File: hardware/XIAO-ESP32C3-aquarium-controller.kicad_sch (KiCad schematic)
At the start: 11 parts, among them J1 Conn_01x07, J3 Conn_01x06, U1 XIAO-ESP32C3, U2 ULN2003, U3 74HC245

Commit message: added new connector, increase copper for al/n
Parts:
- added J2: Conn_01x03, Connector_PinHeader_2.54mm:PinHeader_1x05_P2.54mm_Vertical, symbol Connector_Generic:Conn_01x05
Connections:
- net +5V: now also J2.1 (Pin_1)
- net GND: now also J2.5 (Pin_5)
- net D2: now reaches U1.3 (PA10_A2_D2)
- net D2: now also J2.3 (Pin_3)
- net D6: now reaches U1.7 (PB08_A6_D6_TX)
- net D6: now also J2.4 (Pin_4)
- net D7: now reaches U1.8 (PB09_A7_D7_RX)
- net D7: now also J2.2 (Pin_2)
- no-connect marks 9 -> 6
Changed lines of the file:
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@@
   )
   (no_connect (at 144.78 121.92))
-  (no_connect (at 29.21 86.36))
   (no_connect (at 144.78 124.46))
   (no_connect (at 120.65 72.39))
-  (no_connect (at 29.21 101.6))
-  (no_connect (at 78.74 101.6))
   (no_connect (at 140.97 72.39))
   (no_connect (at 119.38 121.92))
@@
     (stroke (width 0) (type default))
   )
+  (wire (pts (xy 45.72 138.43) (xy 45.72 134.62))
+    (stroke (width 0) (type default))
+  )
+  (wire (pts (xy 45.72 121.92) (xy 45.72 124.46))
+    (stroke (width 0) (type default))
+  )
   (wire (pts (xy 119.38 116.84) (xy 119.38 119.38))
     (stroke (width 0) (type default))
@@
     (stroke (width 0) (type default))
   )
+  (wire (pts (xy 45.72 124.46) (xy 50.8 124.46))
+    (stroke (width 0) (type default))
+  )
   (wire (pts (xy 114.3 116.84) (xy 119.38 116.84))
     (stroke (width 0) (type default))
   )
+  (wire (pts (xy 25.4 86.36) (xy 29.21 86.36))
+    (stroke (width 0) (type default))
+  )
   (wire (pts (xy 222.25 127) (xy 227.33 127))
     (stroke (width 0) (type default))
@@
     (stroke (width 0) (type default))
   )
+  (wire (pts (xy 45.72 132.08) (xy 50.8 132.08))
+    (stroke (width 0) (type default))
+  )
+  (wire (pts (xy 78.74 101.6) (xy 82.55 101.6))
+    (stroke (width 0) (type default))
+  )
   (wire (pts (xy 219.71 119.38) (xy 227.33 119.38))
     (stroke (width 0) (type default))
@@
     (stroke (width 0) (type default))
   )
+  (wire (pts (xy 45.72 127) (xy 50.8 127))
+    (stroke (width 0) (type default))
+  )
   (wire (pts (xy 130.81 78.74) (xy 130.81 77.47))
     (stroke (width 0) (type default))
@@
     (stroke (width 0) (type default))
   )
+  (wire (pts (xy 45.72 134.62) (xy 50.8 134.62))
+    (stroke (width 0) (type default))
+  )
   (wire (pts (xy 119.38 69.85) (xy 119.38 67.31))
     (stroke (width 0) (type default))
@@
     (stroke (width 0) (type default))
   )
+  (wire (pts (xy 25.4 101.6) (xy 29.21 101.6))
+    (stroke (width 0) (type default))
+  )
   (wire (pts (xy 78.74 72.39) (xy 88.9 72.39))
     (stroke (width 0) (type default))
@@
     (stroke (width 0) (type default))
   )
+  (wire (pts (xy 45.72 129.54) (xy 50.8 129.54))
+    (stroke (width 0) (type default))
+  )
   (wire (pts (xy 119.38 132.08) (xy 119.38 139.7))
     (stroke (width 0) (type default))
@@
     (stroke (width 0) (type default))
   )
+  (label "D7" (at 45.72 127 0) (fields_autoplaced)
+    (effects (font (size 1.27 1.27)) (justify left bottom))
+  )
   (label "TS1" (at 177.8 25.4 0) (fields_autoplaced)
     (effects (font (size 1.27 1.27)) (justify left bottom))
@@
     (effects (font (size 1.27 1.27)) (justify left bottom))
   )
+  (label "D6" (at 25.4 101.6 0) (fields_autoplaced)
+    (effects (font (size 1.27 1.27)) (justify left bottom))
+  )
   (label "rel2" (at 177.8 68.58 0) (fields_autoplaced)
     (effects (font (size 1.27 1.27)) (justify left bottom))
@@
     (effects (font (size 1.27 1.27)) (justify left bottom))
   )
+  (label "D2" (at 25.4 86.36 0) (fields_autoplaced)
+    (effects (font (size 1.27 1.27)) (justify left bottom))
+  )
+  (label "D6" (at 45.72 132.08 0) (fields_autoplaced)
+    (effects (font (size 1.27 1.27)) (justify left bottom))
+  )
   (label "RS5" (at 115.57 67.31 0) (fields_autoplaced)
     (effects (font (size 1.27 1.27)) (justify left bottom))
@@
     (effects (font (size 1.27 1.27)) (justify left bottom))
   )
+  (label "D7" (at 82.55 101.6 0) (fields_autoplaced)
+    (effects (font (size 1.27 1.27)) (justify left bottom))
+  )
   (label "rel3" (at 143.51 67.31 0) (fields_autoplaced)
     (effects (font (size 1.27 1.27)) (justify left bottom))
@@
   )
   (label "RS1" (at 114.3 116.84 0) (fields_autoplaced)
+    (effects (font (size 1.27 1.27)) (justify left bottom))
+  )
+  (label "D2" (at 45.72 129.54 0) (fields_autoplaced)
     (effects (font (size 1.27 1.27)) (justify left bottom))
   )
@@
     )
   )
+  (symbol (lib_id "power:GND") (at 45.72 138.43 0) (unit 1)
+    (in_bom yes) (on_board yes) (dnp no) (fields_autoplaced)
+    (property "Reference" "#PWR0103" (at 45.72 144.78 0)
+      (effects (font (size 1.27 1.27)) hide)
+    )
+    (property "Value" "GND" (at 45.72 143.51 0)
+      (effects (font (size 1.27 1.27)))
+    )
+    (property "Footprint" "" (at 45.72 138.43 0)
+      (effects (font (size 1.27 1.27)) hide)
+    )
+    (property "Datasheet" "" (at 45.72 138.43 0)
+      (effects (font (size 1.27 1.27)) hide)
+    )
+    (pin "1")
+    (instances
+      (project "AquariumController"
+        (path "/75069d71-4fd1-4b49-820b-d8e60608591a"
+          (reference "#PWR0103") (unit 1)
+        )
+        (path "/75069d71-4fd1-4b49-820b-d8e60608591a/cae2cbae-b73f-4926-bf8f-e52abe478c81"
+          (reference "#PWR017") (unit 1)
+        )
+      )
+      (project "XIAO-ESP32C3-aquarium-controller"
+        (path "/e16639bd-7ef7-40a4-9337-f1b4c79f775b/bee5e875-31e5-4be6-8420-aaa58bd7d71a"
+          (reference "#PWR02") (unit 1)
+        )
+        (path "/e16639bd-7ef7-40a4-9337-f1b4c79f775b"
+          (reference "#PWR035") (unit 1)
+        )
+      )
+    )
+  )
   (symbol (lib_id "Device:C") (at 137.16 34.29 90) (unit 1)
     (in_bom yes) (on_board yes) (dnp no) (fields_autoplaced)
@@
         (path "/e16639bd-7ef7-40a4-9337-f1b4c79f775b"
           (reference "H1") (unit 1)
+        )
+      )
+    )
+  )
+  (symbol (lib_id "Connector_Generic:Conn_01x05") (at 55.88 129.54 0) (unit 1)
+    (in_bom no) (on_board yes) (dnp no) (fields_autoplaced)
+    (property "Reference" "J2" (at 58.42 128.27 0)
+      (effects (font (size 1.27 1.27)) (justify left))
+    )
+    (property "Value" "Conn_01x03" (at 58.42 130.81 0)
+      (effects (font (size 1.27 1.27)) (justify left))
+    )
+    (property "Footprint" "Connector_PinHeader_2.54mm:PinHeader_1x05_P2.54mm_Vertical" (at 55.88 129.54 0)
+      (effects (font (size 1.27 1.27)) hide)
+    )
+    (property "Datasheet" "~" (at 55.88 129.54 0)
+      (effects (font (size 1.27 1.27)) hide)
+    )
+    (property "JLCPCB Part #" "" (at 55.88 129.54 0)
+      (effects (font (size 1.27 1.27)) hide)
+    )
+    (pin "1")
+    (pin "2")
+    (pin "3")
+    (pin "4")
+    (pin "5")
+    (instances
+      (project "AquariumController"
+        (path "/75069d71-4fd1-4b49-820b-d8e60608591a/5fd9d187-6c53-4498-b6f0-99546b3ca792"
+          (reference "J2") (unit 1)
+        )
+      )
+      (project "XIAO-ESP32C3-aquarium-controller"
+        (path "/e16639bd-7ef7-40a4-9337-f1b4c79f775b/6cb334e1-33ef-41c6-b7ff-62ff02100eaa"
+          (reference "J4") (unit 1)
+        )
+        (path "/e16639bd-7ef7-40a4-9337-f1b4c79f775b"
+          (reference "J5") (unit 1)
         )
       )
@@
         )
       )
+    )
+  )
+  (symbol (lib_id "power:+5V") (at 45.72 121.92 0) (unit 1)
+    (in_bom yes) (on_board yes) (dnp no) (fields_autoplaced)
+    (property "Reference" "#PWR0102" (at 45.72 125.73 0)
+      (effects (font (size 1.27 1.27)) hide)
+    )
+    (property "Value" "+5V" (at 45.72 116.84 0)
+      (effects (font (size 1.27 1.27)))
+    )
+    (property "Footprint" "" (at 45.72 121.92 0)
+      (effects (font (size 1.27 1.27)) hide)
+    )
+    (property "Datasheet" "" (at 45.72 121.92 0)
+      (effects (font (size 1.27 1.27)) hide)
+    )
+    (pin "1")
+    (instances
+      (project "AquariumController"
+        (path "/75069d71-4fd1-4b49-820b-d8e60608591a"
+          (reference "#PWR0102") (unit 1)
+        )
+        (path "/75069d71-4fd1-4b49-820b-d8e60608591a/cae2cbae-b73f-4926-bf8f-e52abe478c81"
+          (reference "#PWR016") (unit 1)
+        )
+      )
+      (project "XIAO-ESP32C3-aquarium-controller"
+        (path "/e16639bd-7ef7-40a4-9337-f1b4c79f775b/bee5e875-31e5-4be6-8420-aaa58bd7d71a"
+          (reference "#PWR01") (unit 1)
+        )
+        (path "/e16639bd-7ef7-40a4-9337-f1b4c79f775b"
+          (reference "#PWR034") (unit 1)
+        )
+      )

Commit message: 3v3 instead 5v on connector
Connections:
- net +3.3V: now also J2.1 (Pin_1)
- net +5V: no longer J2.1 (Pin_1)
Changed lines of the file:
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@@
+    )
+  )
+  (symbol (lib_id "power:+3.3V") (at 45.72 121.92 0) (unit 1)
+    (in_bom yes) (on_board yes) (dnp no) (fields_autoplaced)
+    (property "Reference" "#PWR029" (at 45.72 125.73 0)
+      (effects (font (size 1.27 1.27)) hide)
+    )
+    (property "Value" "+3.3V" (at 45.72 118.11 0)
+      (effects (font (size 1.27 1.27)))
+    )
+    (property "Footprint" "" (at 45.72 121.92 0)
+      (effects (font (size 1.27 1.27)) hide)
+    )
+    (property "Datasheet" "" (at 45.72 121.92 0)
+      (effects (font (size 1.27 1.27)) hide)
+    )
+    (pin "1")
+    (instances
+      (project "AquariumController"
+        (path "/75069d71-4fd1-4b49-820b-d8e60608591a/cae2cbae-b73f-4926-bf8f-e52abe478c81"
+          (reference "#PWR029") (unit 1)
+        )
+        (path "/75069d71-4fd1-4b49-820b-d8e60608591a"
+          (reference "#PWR031") (unit 1)
+        )
+        (path "/75069d71-4fd1-4b49-820b-d8e60608591a/5fd9d187-6c53-4498-b6f0-99546b3ca792"
+          (reference "#PWR014") (unit 1)
+        )
+      )
+      (project "XIAO-ESP32C3-aquarium-controller"
+        (path "/e16639bd-7ef7-40a4-9337-f1b4c79f775b/6cb334e1-33ef-41c6-b7ff-62ff02100eaa"
+          (reference "#PWR029") (unit 1)
+        )
+        (path "/e16639bd-7ef7-40a4-9337-f1b4c79f775b"
+          (reference "#PWR034") (unit 1)
+        )
+      )
     )
   )
@@
         )
       )
-    )
-  )
-  (symbol (lib_id "power:+5V") (at 45.72 121.92 0) (unit 1)
-    (in_bom yes) (on_board yes) (dnp no) (fields_autoplaced)
-    (property "Reference" "#PWR0102" (at 45.72 125.73 0)
-      (effects (font (size 1.27 1.27)) hide)
-    )
-    (property "Value" "+5V" (at 45.72 116.84 0)
-      (effects (font (size 1.27 1.27)))
-    )
-    (property "Footprint" "" (at 45.72 121.92 0)
-      (effects (font (size 1.27 1.27)) hide)
-    )
-    (property "Datasheet" "" (at 45.72 121.92 0)
-      (effects (font (size 1.27 1.27)) hide)
-    )
-    (pin "1")
-    (instances
-      (project "AquariumController"
-        (path "/75069d71-4fd1-4b49-820b-d8e60608591a"
-          (reference "#PWR0102") (unit 1)
-        )
-        (path "/75069d71-4fd1-4b49-820b-d8e60608591a/cae2cbae-b73f-4926-bf8f-e52abe478c81"
-          (reference "#PWR016") (unit 1)
-        )
-      )
-      (project "XIAO-ESP32C3-aquarium-controller"
-        (path "/e16639bd-7ef7-40a4-9337-f1b4c79f775b/bee5e875-31e5-4be6-8420-aaa58bd7d71a"
-          (reference "#PWR01") (unit 1)
-        )
-        (path "/e16639bd-7ef7-40a4-9337-f1b4c79f775b"
-          (reference "#PWR034") (unit 1)
-        )
-      )

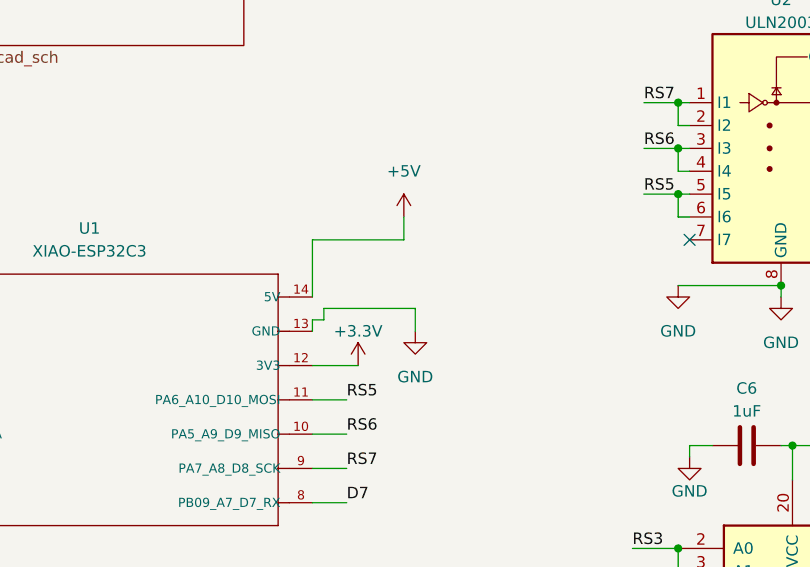
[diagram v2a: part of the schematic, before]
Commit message: capacitor for ESP32C3
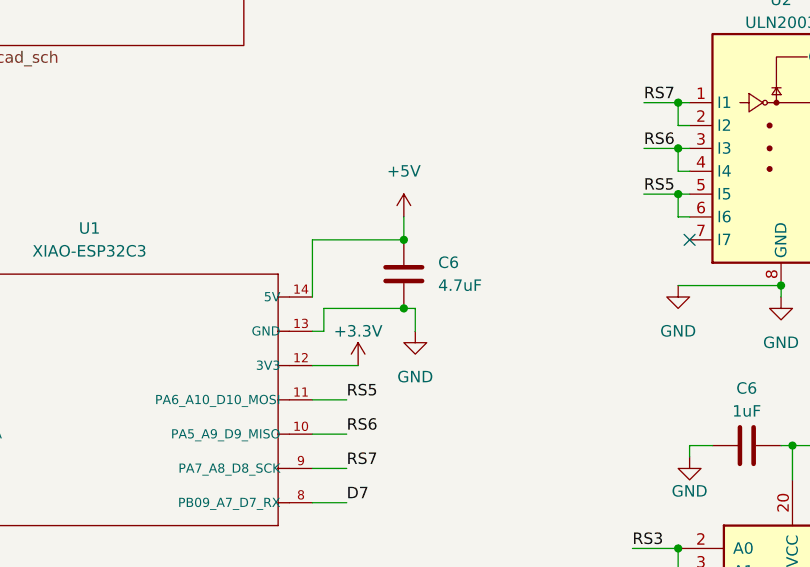
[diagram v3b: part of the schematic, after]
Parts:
- added C6: 4.7uF, Capacitor_SMD:C_0402_1005Metric, symbol Device:C
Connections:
- net +5V: now also C6.2
- net GND: now also C6.1
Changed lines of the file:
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@@
   (junction (at 119.38 57.15) (diameter 0) (color 0 0 0 0)
   )
+  (junction (at 88.9 72.39) (diameter 0) (color 0 0 0 0)
+  )
   (junction (at 119.38 106.68) (diameter 0) (color 0 0 0 0)
   )
@@
   )
   (junction (at 144.78 111.76) (diameter 0) (color 0 0 0 0)
+  )
+  (junction (at 88.9 80.01) (diameter 0) (color 0 0 0 0)
   )
   (junction (at 142.24 62.23) (diameter 0) (color 0 0 0 0)
@@
     (stroke (width 0) (type default))
   )
+  (wire (pts (xy 88.9 80.01) (xy 90.17 80.01))
+    (stroke (width 0) (type default))
+  )
   (wire (pts (xy 143.51 67.31) (xy 142.24 67.31))
     (stroke (width 0) (type default))
@@
     (stroke (width 0) (type default))
   )
-  (wire (pts (xy 78.74 81.28) (xy 78.74 82.55))
+  (wire (pts (xy 80.01 80.01) (xy 80.01 82.55))
     (stroke (width 0) (type default))
   )
@@
     (stroke (width 0) (type default))
   )
+  (wire (pts (xy 80.01 82.55) (xy 78.74 82.55))
+    (stroke (width 0) (type default))
+  )
   (wire (pts (xy 204.47 85.09) (xy 220.98 85.09))
     (stroke (width 0) (type default))
@@
     (stroke (width 0) (type default))
   )
-  (wire (pts (xy 80.01 81.28) (xy 78.74 81.28))
-    (stroke (width 0) (type default))
-  )
   (wire (pts (xy 219.71 106.68) (xy 219.71 119.38))
     (stroke (width 0) (type default))
@@
     (stroke (width 0) (type default))
   )
-  (wire (pts (xy 80.01 80.01) (xy 90.17 80.01))
+  (wire (pts (xy 80.01 80.01) (xy 88.9 80.01))
     (stroke (width 0) (type default))
   )
@@
   )
   (wire (pts (xy 132.08 95.25) (xy 148.59 95.25))
-    (stroke (width 0) (type default))
-  )
-  (wire (pts (xy 80.01 81.28) (xy 80.01 80.01))
     (stroke (width 0) (type default))
   )
@@
         )
       )
+    )
+  )
+  (symbol (lib_id "Device:C") (at 88.9 76.2 180) (unit 1)
+    (in_bom yes) (on_board yes) (dnp no) (fields_autoplaced)
+    (property "Reference" "C6" (at 92.71 74.93 0)
+      (effects (font (size 1.27 1.27)) (justify right))
+    )
+    (property "Value" "4.7uF" (at 92.71 77.47 0)
+      (effects (font (size 1.27 1.27)) (justify right))
+    )
+    (property "Footprint" "Capacitor_SMD:C_0402_1005Metric" (at 87.9348 72.39 0)
+      (effects (font (size 1.27 1.27)) hide)
+    )
+    (property "Datasheet" "~" (at 88.9 76.2 0)
+      (effects (font (size 1.27 1.27)) hide)
+    )
+    (property "JLCPCB Part #" "C23733" (at 88.9 76.2 0)
+      (effects (font (size 1.27 1.27)) hide)
+    )
+    (pin "1")
+    (pin "2")
+    (instances
+      (project "AquariumController"
+        (path "/75069d71-4fd1-4b49-820b-d8e60608591a"
+          (reference "C6") (unit 1)
+        )
+      )
+      (project "XIAO-ESP32C3-aquarium-controller"
+        (path "/e16639bd-7ef7-40a4-9337-f1b4c79f775b"
+          (reference "C13") (unit 1)
+        )
+      )

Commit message: change hole size
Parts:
- H1, H2, H3, H4: footprint MountingHole:MountingHole_2.7mm_M2.5 -> ProjectLibrary:MountingHole_2.8mm_M2.6
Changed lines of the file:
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@@
       (effects (font (size 1.27 1.27)) (justify left) hide)
     )
-    (property "Footprint" "MountingHole:MountingHole_2.7mm_M2.5" (at 20.32 191.77 0)
+    (property "Footprint" "ProjectLibrary:MountingHole_2.8mm_M2.6" (at 20.32 191.77 0)
       (effects (font (size 1.27 1.27)) hide)
     )
@@
       (effects (font (size 1.27 1.27)) (justify left) hide)
     )
-    (property "Footprint" "MountingHole:MountingHole_2.7mm_M2.5" (at 20.32 186.69 0)
+    (property "Footprint" "ProjectLibrary:MountingHole_2.8mm_M2.6" (at 20.32 186.69 0)
       (effects (font (size 1.27 1.27)) hide)
     )
@@
       (effects (font (size 1.27 1.27)) (justify left) hide)
     )
-    (property "Footprint" "MountingHole:MountingHole_2.7mm_M2.5" (at 20.32 176.53 0)
+    (property "Footprint" "ProjectLibrary:MountingHole_2.8mm_M2.6" (at 20.32 176.53 0)
       (effects (font (size 1.27 1.27)) hide)
     )
@@
       (effects (font (size 1.27 1.27)) (justify left) hide)
     )
-    (property "Footprint" "MountingHole:MountingHole_2.7mm_M2.5" (at 20.32 181.61 0)
-      (effects (font (size 1.27 1.27)) hide)
-    )
+    (property "Footprint" "ProjectLibrary:MountingHole_2.8mm_M2.6" (at 20.32 181.61 0)
+      (effects (font (size 1.27 1.27)) hide)
+    )

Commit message: labeling
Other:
- note added: "High Voltage"
- title: (none) -> XIAO ESP32C3 Aquarium Controller
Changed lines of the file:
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@@
 (kicad_sch (version 20230121) (generator eeschema)
   (paper "A4")
+  (title_block
+    (title "XIAO ESP32C3 Aquarium Controller")
+  )
   (junction (at 119.38 57.15) (diameter 0) (color 0 0 0 0)
   )
@@
     (stroke (width 0) (type default))
   )
+  (rectangle (start 199.39 43.18) (end 247.65 91.44)
+    (stroke (width 0) (type default))
+    (fill (type none))
+  )
+  (text "High Voltage" (at 229.87 49.53 0)
+    (effects (font (size 1.27 1.27)) (justify left bottom))
+  )
   (label "D7" (at 45.72 127 0) (fields_autoplaced)

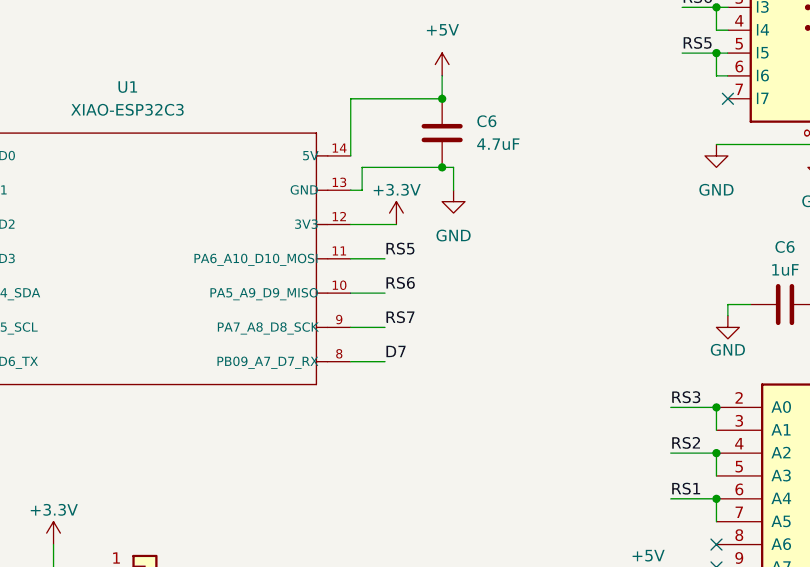
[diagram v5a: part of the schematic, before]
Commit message: fix after new footprint
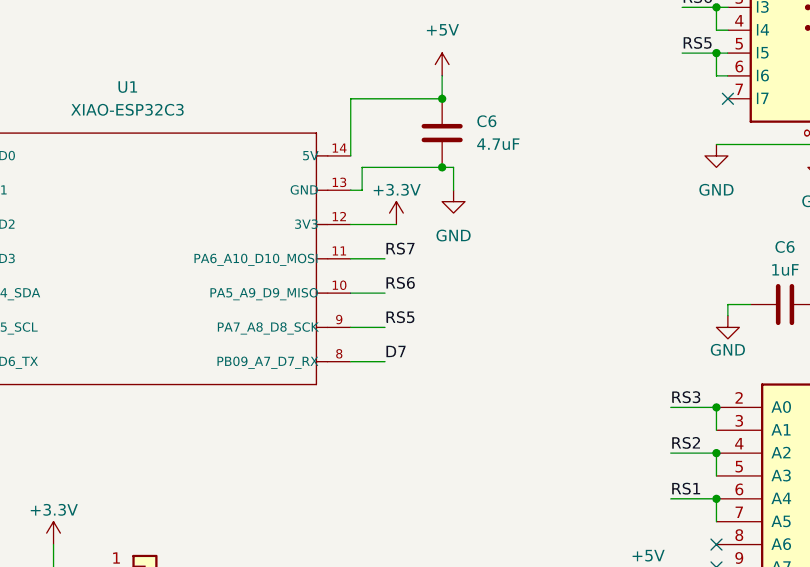
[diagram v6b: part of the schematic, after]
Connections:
- net RS5: now also U1.9 (PA7_A8_D8_SCK); no longer U1.11 (PA6_A10_D10_MOSI)
- net RS7: now also U1.11 (PA6_A10_D10_MOSI); no longer U1.9 (PA7_A8_D8_SCK)
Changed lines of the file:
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@@
     (effects (font (size 1.27 1.27)) (justify left bottom))
   )
-  (label "RS5" (at 82.55 90.17 0) (fields_autoplaced)
+  (label "RS7" (at 82.55 90.17 0) (fields_autoplaced)
     (effects (font (size 1.27 1.27)) (justify left bottom))
   )
@@
     (effects (font (size 1.27 1.27)) (justify left bottom))
   )
-  (label "RS7" (at 82.55 97.79 0) (fields_autoplaced)
+  (label "RS5" (at 82.55 97.79 0) (fields_autoplaced)
     (effects (font (size 1.27 1.27)) (justify left bottom))
   )
